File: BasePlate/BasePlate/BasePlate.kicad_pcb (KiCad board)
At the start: 4 copper layers, 114.9 x 142.2 mm, 10 parts, among them J1 JST_BM04B-GHS-TBT, J2 1586842-6, J3 JST_BM03B-GHS-TBT, J4 JST_BM04B-GHS-TBT, J5 JST_BM04B-GHS-TBT, J6 JST_BM04B-GHS-TBT, J7 JST_BM04B-GHS-TBT, J8 JST_BM04B-GHS-TBT

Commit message: mostly finished
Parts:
- added H1: MountingHole_Pad, TestPoint:TestPoint_Pad_D4.0mm, F.Cu at (33.5, 110.2)
- added H2: MountingHole_Pad, TestPoint:TestPoint_Pad_D4.0mm, F.Cu at (36.8, 119.2)
- added H3: MountingHole_Pad, TestPoint:TestPoint_Pad_D4.0mm, F.Cu at (119.6, 119.6)
- added H4: MountingHole_Pad, TestPoint:TestPoint_Pad_D4.0mm, F.Cu at (123.2, 110.2)
- added H5: MountingHole_Pad, TestPoint:TestPoint_Pad_D4.0mm, F.Cu at (106.6, 80.0)
- added H6: MountingHole_Pad, TestPoint:TestPoint_Pad_D4.0mm, F.Cu at (100.8, 74.0)
- added H7: MountingHole_Pad, TestPoint:TestPoint_Pad_D4.0mm, F.Cu at (56.1, 74.4)
- added H8: MountingHole_Pad, TestPoint:TestPoint_Pad_D4.0mm, F.Cu at (51.0, 80.2)
- added J9: Conn_01x02_Socket, Connector_PinSocket_2.54mm:PinSocket_1x02_P2.54mm_Vertical, F.Cu at (109.8, 158.3)
- J8: value JST_BM04B-GHS-TBT -> Conn_01x03_Socket; footprint bots:JST_BM04B-GHS-TBT -> Connector_PinSocket_2.54mm:PinSocket_1x03_P2.54mm_Vertical
- moved J8 45.9 mm to (47.7, 156.2), turned to 0 degrees
- moved J4 25.9 mm to (43.4, 110.4), turned to -90 degrees
- moved R1 0.25 mm to (94.8, 42.8)
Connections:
- J1 pad 2: CAN+ -> /CAN_P
- J1 pad 3: CAN- -> /CAN_N
- J4 pad 2: unconnected-(J4-Pad2) -> /CAN_P
- J4 pad 3: unconnected-(J4-Pad3) -> /CAN_N
- J5 pad 2: unconnected-(J5-Pad2) -> /CAN_P
- J5 pad 3: unconnected-(J5-Pad3) -> /CAN_N
- J6 pad 2: unconnected-(J6-Pad2) -> /CAN_P
- J6 pad 3: unconnected-(J6-Pad3) -> /CAN_N
- J7 pad 2: unconnected-(J7-Pad2) -> /CAN_P
- J7 pad 3: unconnected-(J7-Pad3) -> /CAN_N
- J8 pad 1: GND -> BKBM
- J8 pad 2: unconnected-(J8-Pad2) -> +5V
- J8 pad 3: unconnected-(J8-Pad3) -> GND
- JP1 pad 1: CAN+ -> /CAN_P
- R1 pad 2: CAN- -> /CAN_N
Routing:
- net +5V: track 0.00 -> 275.5 mm, vias 0 -> 1
- net /CAN_P: track 0.00 -> 207.1 mm, vias 0 -> 4
- net /CAN_N: track 0.00 -> 201.5 mm, vias 0 -> 4
- net BKBM: track 0.00 -> 128.2 mm, vias 0 -> 1
- net GND: track 3.67 -> 21.8 mm, vias 72 -> 103
- net CAN+: track 14.2 -> 0.00 mm
- net CAN-: track 9.46 -> 0.00 mm
- net VCC: vias 70 -> 90

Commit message: baseplate updates
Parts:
- moved JP1 83.6 mm to (110.8, 119.2), turned to 90 degrees
- moved R1 81.1 mm to (111.0, 122.2)
- moved J5 1.09 mm to (114.5, 110.5)
- moved J6 1.09 mm to (114.5, 94.1)
- moved J4 0.86 mm to (42.5, 110.4)
- moved J7 0.71 mm to (42.6, 94.1)
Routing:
- net +5V: track 275.5 -> 256.3 mm
- net /CAN_N: track 201.5 -> 209.4 mm, vias 4 -> 2
- net BKBM: track 128.2 -> 124.0 mm
- net /CAN_P: track 207.1 -> 210.2 mm, vias 4 -> 2
- net GND: track 21.8 -> 21.2 mm

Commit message: baseplate
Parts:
- H1, H2, H3, H4, H5, H6, H7, H8: value MountingHole_Pad -> SMD_Pad_VBAT; footprint TestPoint:TestPoint_Pad_D4.0mm -> thebots_baseplate:TestPoint_Pad_D4.0mm
- JP1: value Jumper_2_Bridged -> Jumper_2_Bridged_smd; footprint Connector_PinHeader_2.54mm:PinHeader_1x02_P2.54mm_Vertical -> thebots_baseplate:PinHeader_1x02_P2.54mm_Vertical_SMD_Pin1Left
- moved R1 9.76 mm to (113.7, 131.5)
- moved JP1 8.28 mm to (114.0, 126.9)
- moved H6 5.18 mm to (95.6, 73.7)
- moved H7 5.10 mm to (61.2, 73.7)
- moved H5 3.73 mm to (103.0, 81.0)
- moved J6 3.34 mm to (116.8, 91.7), turned to 135 degrees
- moved J7 3.14 mm to (40.7, 91.7), turned to -135 degrees
- moved H8 2.89 mm to (53.8, 81.0)
- moved J5 1.97 mm to (116.0, 111.8), turned to 65 degrees
- moved J4 1.70 mm to (41.5, 111.8), turned to -65 degrees
- moved H4 1.01 mm to (124.2, 110.3)
- moved H3 0.71 mm to (120.1, 119.1)
- moved H2 0.59 mm to (37.4, 119.1)
- moved H1 0.21 mm to (33.3, 110.3)
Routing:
- net +5V: track 256.3 -> 13.8 mm, vias 1 -> 2
- net /CAN_N: track 209.4 -> 240.4 mm
- net /CAN_P: track 210.2 -> 240.2 mm
- net GND: track 21.2 -> 2.51 mm, vias 103 -> 73
- net BKBM: track 124.0 -> 128.6 mm, vias 1 -> 3
- net Net-(JP1-B): track 3.53 -> 6.62 mm
- net VCC: vias 90 -> 70
- added copper zone on F.Cu, net +5V

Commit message: wip baseplate
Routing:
- net BKBM: track 128.6 -> 117.6 mm
- added copper zone on B.Cu, net +5V
- removed copper zone on F.Cu, net +5V
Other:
- outline, holes or cut-outs redrawn

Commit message: wip baseplate mostly done
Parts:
- moved H5 11.1 mm to (111.2, 88.5)
- moved H6 11.1 mm to (103.8, 81.2)
- moved H7 10.6 mm to (53.7, 81.2)
- moved H8 10.6 mm to (46.3, 88.5)
- moved J6 5.14 mm to (120.5, 95.3)
- moved J7 4.82 mm to (37.5, 95.3)
- moved J4 1.00 mm to (42.5, 111.8)
- moved J5 1.00 mm to (115.0, 111.8)
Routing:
- net /CAN_P: track 240.2 -> 258.1 mm
- net /CAN_N: track 240.4 -> 258.0 mm
- net BKBM: track 117.6 -> 133.8 mm, vias 3 -> 4
- net +5V: track 13.8 -> 3.43 mm, vias 2 -> 1

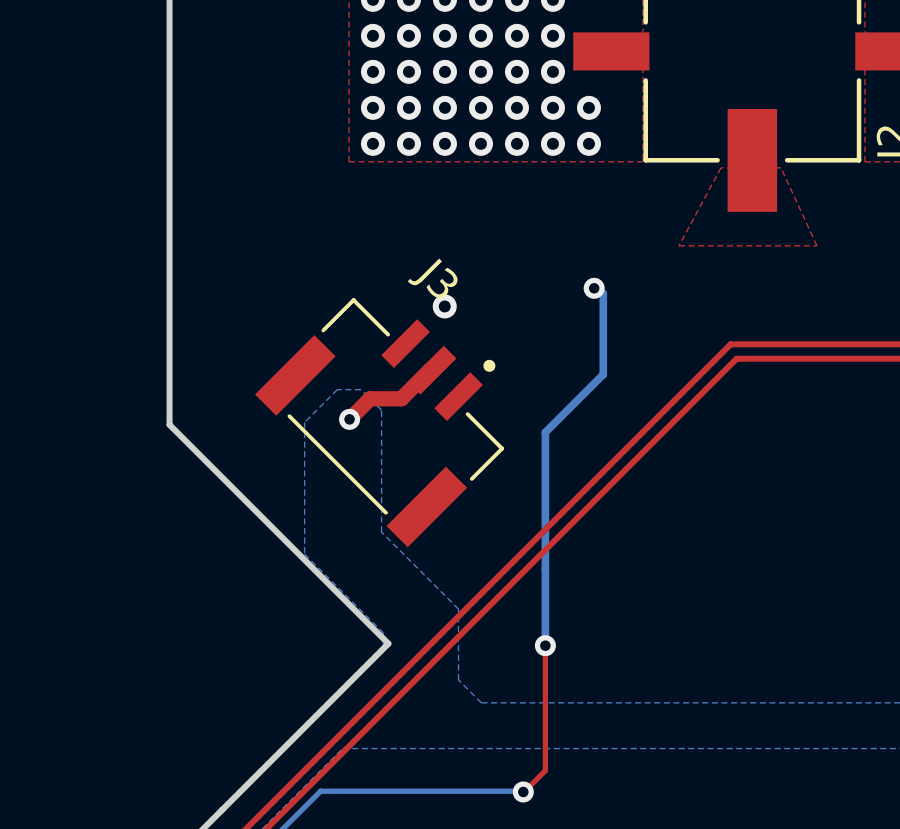
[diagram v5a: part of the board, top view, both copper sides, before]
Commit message: wip breakbeam voltage divider
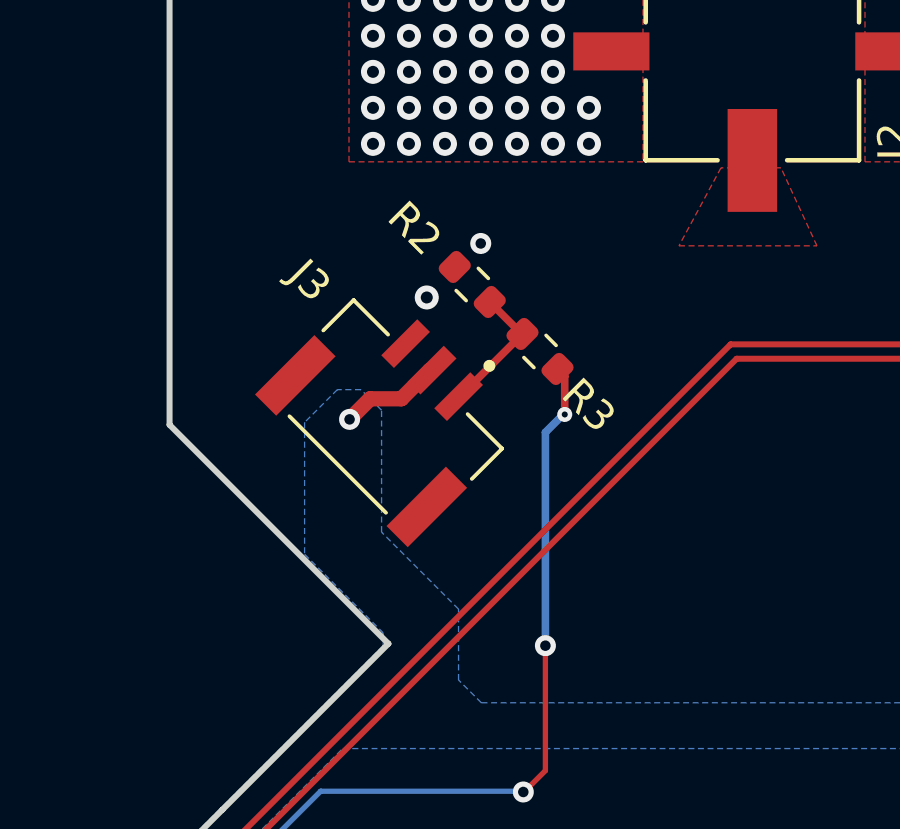
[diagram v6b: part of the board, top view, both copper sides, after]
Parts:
- added R2: 20k, Resistor_SMD:R_0603_1608Metric, F.Cu at (69.3, 45.6)
- added R3: 10k, Resistor_SMD:R_0603_1608Metric, F.Cu at (71.6, 47.8)
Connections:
- J3 pad 1: BKBM -> Net-(J3-Pad1)
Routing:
- net Net-(J3-Pad1): track 0.00 -> 4.67 mm
- net BKBM: track 133.8 -> 130.3 mm
- net GND: vias 73 -> 74

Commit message: baseplate done
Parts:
- added G***: LOGO, LOGO, F.Cu at (109.9, 136.6)
- added G***: LOGO, LOGO, F.Cu at (47.5, 137.2)
- added G***: LOGO, LOGO, F.Cu at (68.8, 66.2)
- moved JP1 2.14 mm to (116.1, 126.7)
- moved R1 1.58 mm to (115.3, 131.6)
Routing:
- net GND: track 2.51 -> 0.18 mm, vias 74 -> 82
- net /CAN_P: track 258.1 -> 259.1 mm
- net /CAN_N: track 258.0 -> 259.0 mm
- net Net-(JP1-B): track 6.62 -> 7.13 mm
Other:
- board text added: "Baseplate V1.0 Designed By: Akhil Veeranghata Henry Bryant Date: March 14th, 2024"

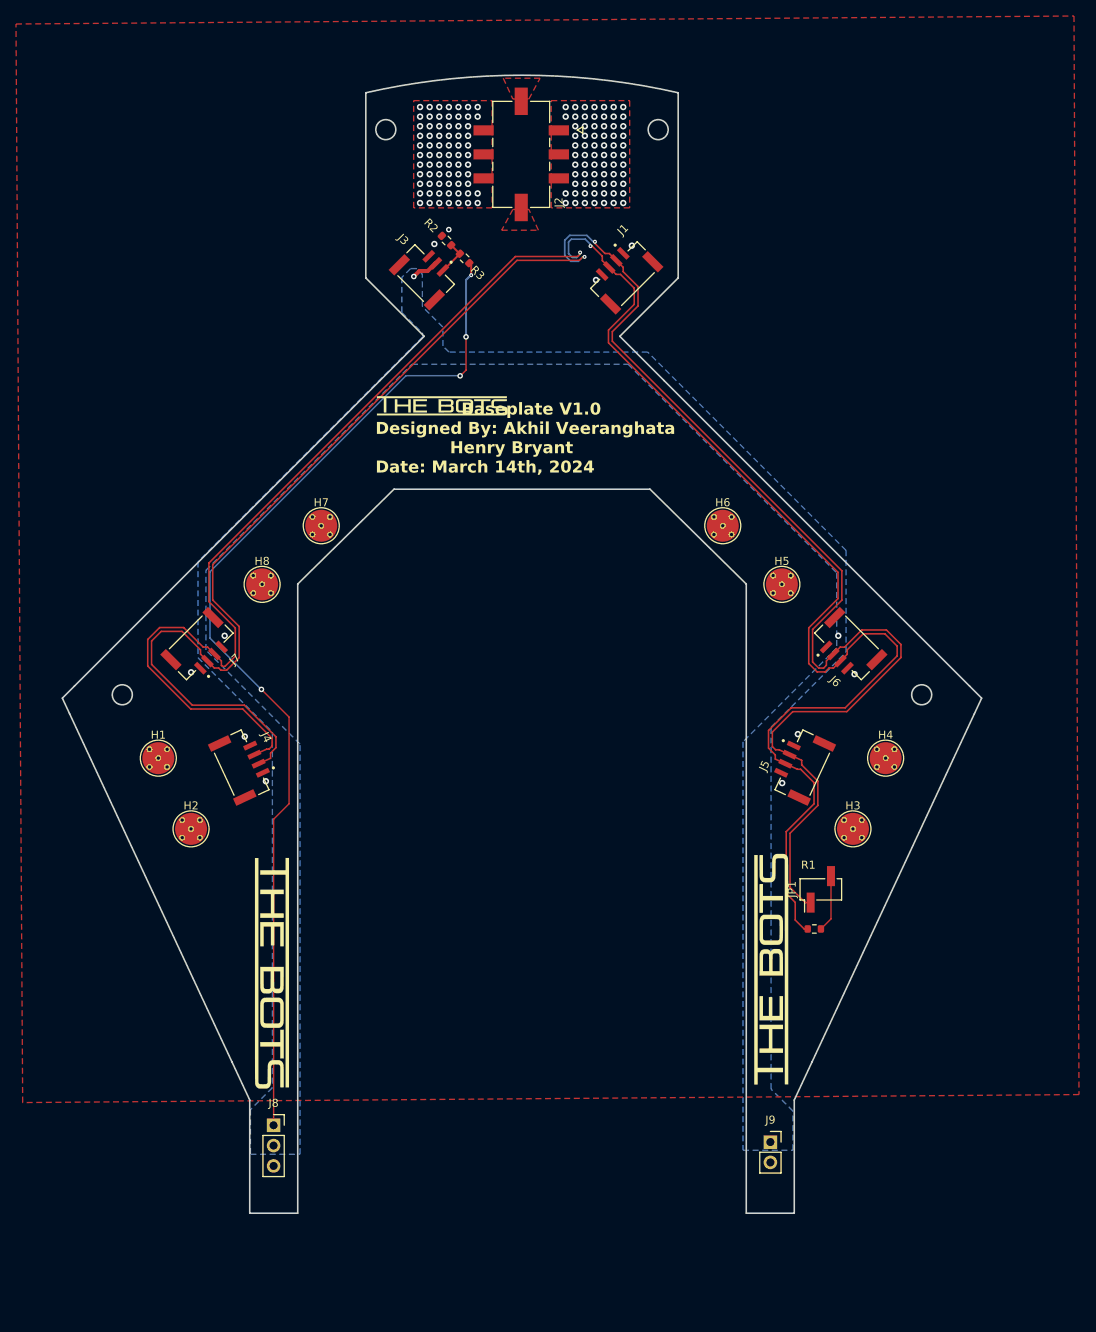
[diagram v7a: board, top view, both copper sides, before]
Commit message: skidplate, then realized its pointless
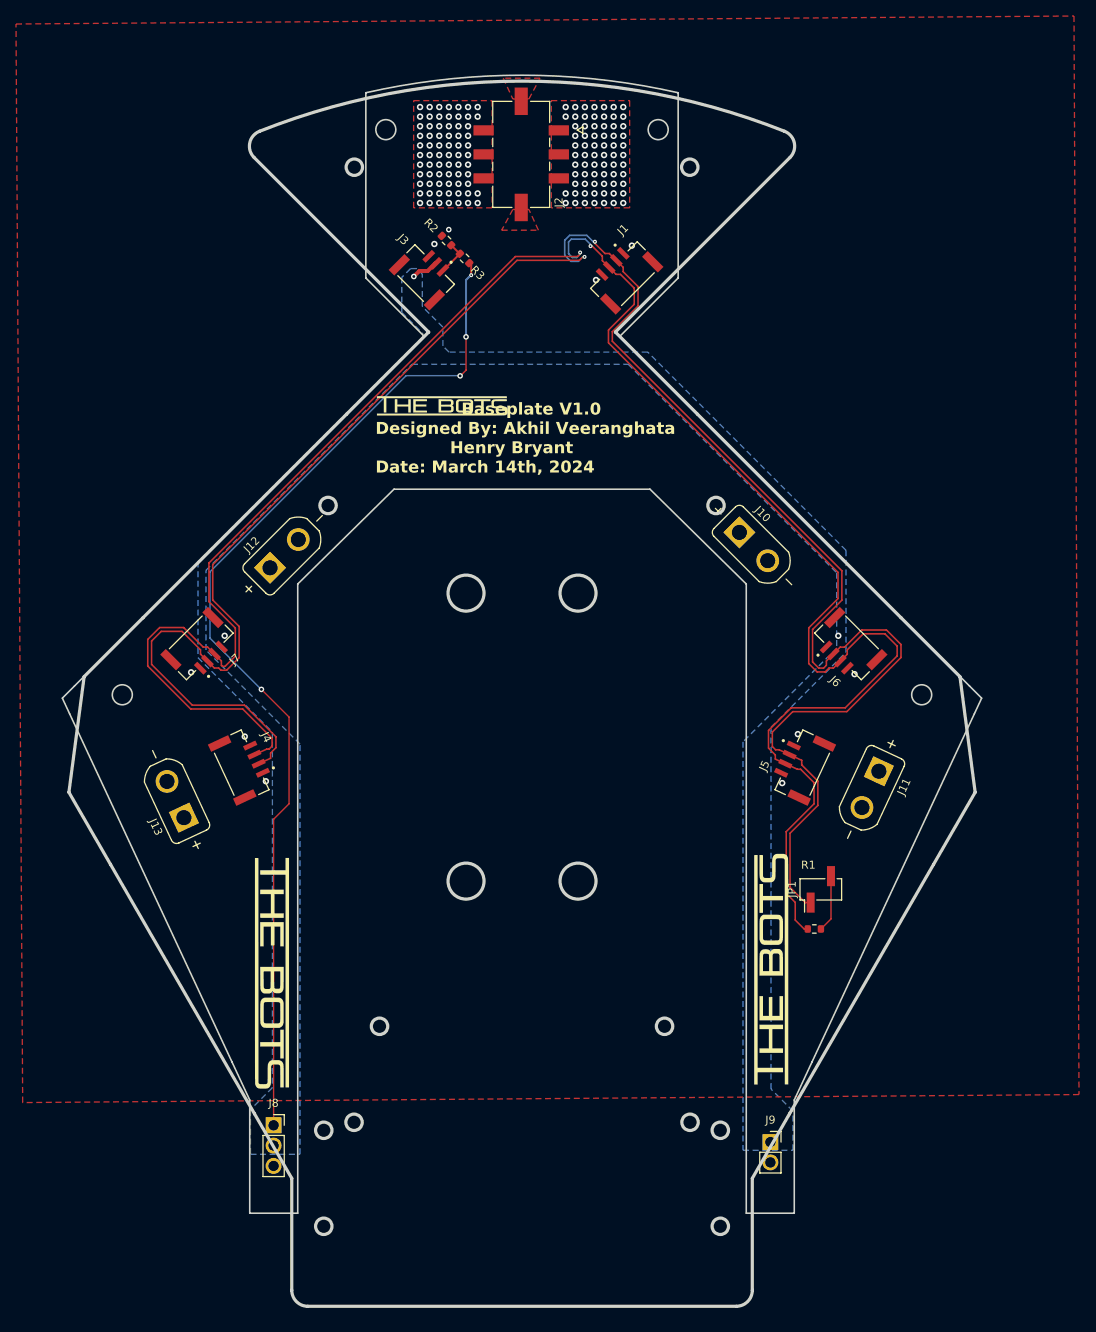
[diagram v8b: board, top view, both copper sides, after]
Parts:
- removed H1, H2, H3, H4, H5, H6, H7, H8: SMD_Pad_VBAT, thebots_baseplate:TestPoint_Pad_D4.0mm
- added J10: XT30UPB-M, bots:AMASS_XT30UPB-M, F.Cu at (107.7, 83.8)
- added J11: XT30UPB-M, bots:AMASS_XT30UPB-M, F.Cu at (122.3, 114.2)
- added J12: XT30UPB-M, bots:AMASS_XT30UPB-M, F.Cu at (49.0, 84.7)
- added J13: XT30UPB-M, bots:AMASS_XT30UPB-M, F.Cu at (35.4, 115.4)
- J8: footprint Connector_PinSocket_2.54mm:PinSocket_1x03_P2.54mm_Vertical -> bots:PinSocket_1x03_P2.54mm_Vertical
- J9: footprint Connector_PinSocket_2.54mm:PinSocket_1x02_P2.54mm_Vertical -> bots:PinSocket_1x02_P2.54mm_Vertical
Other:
- board size 114.9 x 142.2 mm -> 114.9 x 153.9 mm
